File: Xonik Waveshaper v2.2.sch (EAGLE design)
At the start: 96 parts, among them IC1 TL074JT, IC2 TL074JT, IC3 TL074JT, IC4 TL072JT, IC5 4013T, IC6 LM311T, T1 2n3904

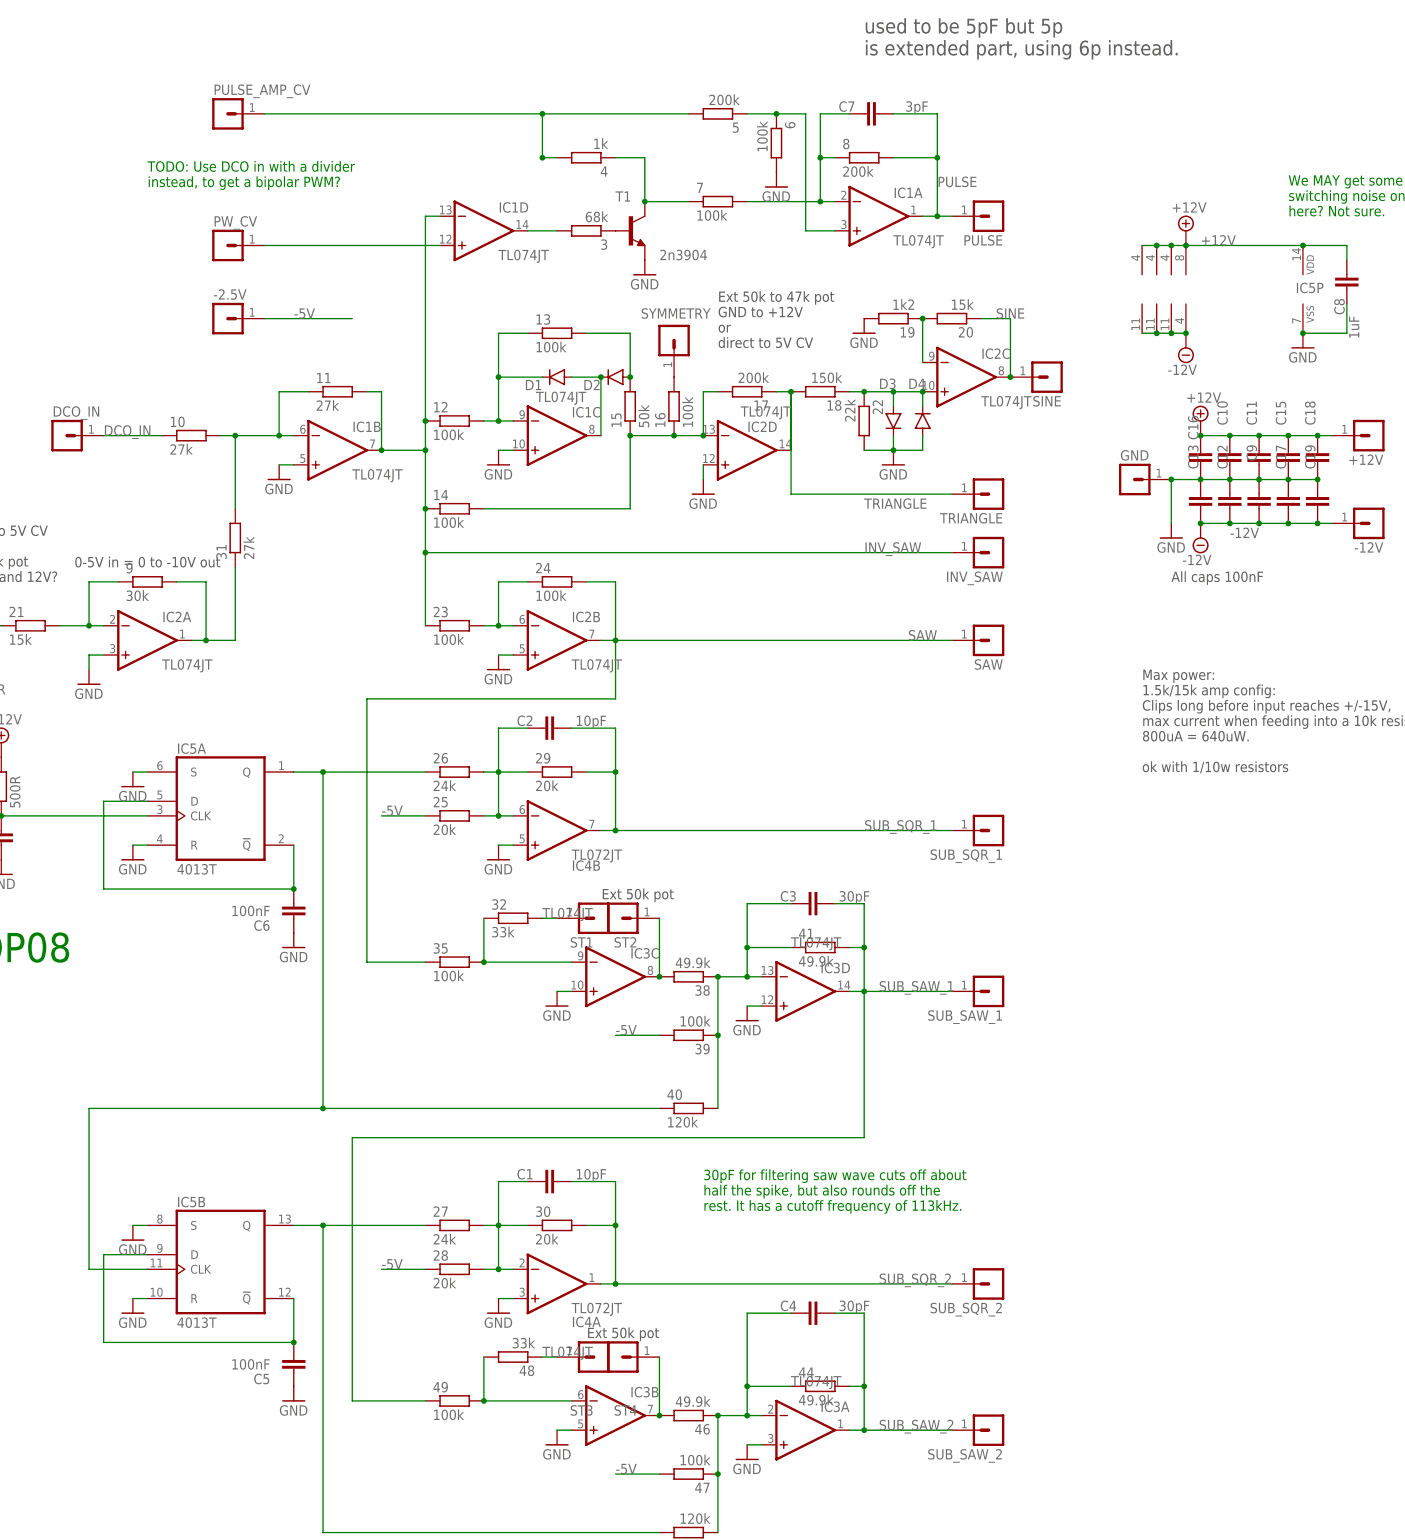
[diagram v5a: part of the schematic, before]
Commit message: Updated with bipolar pwm
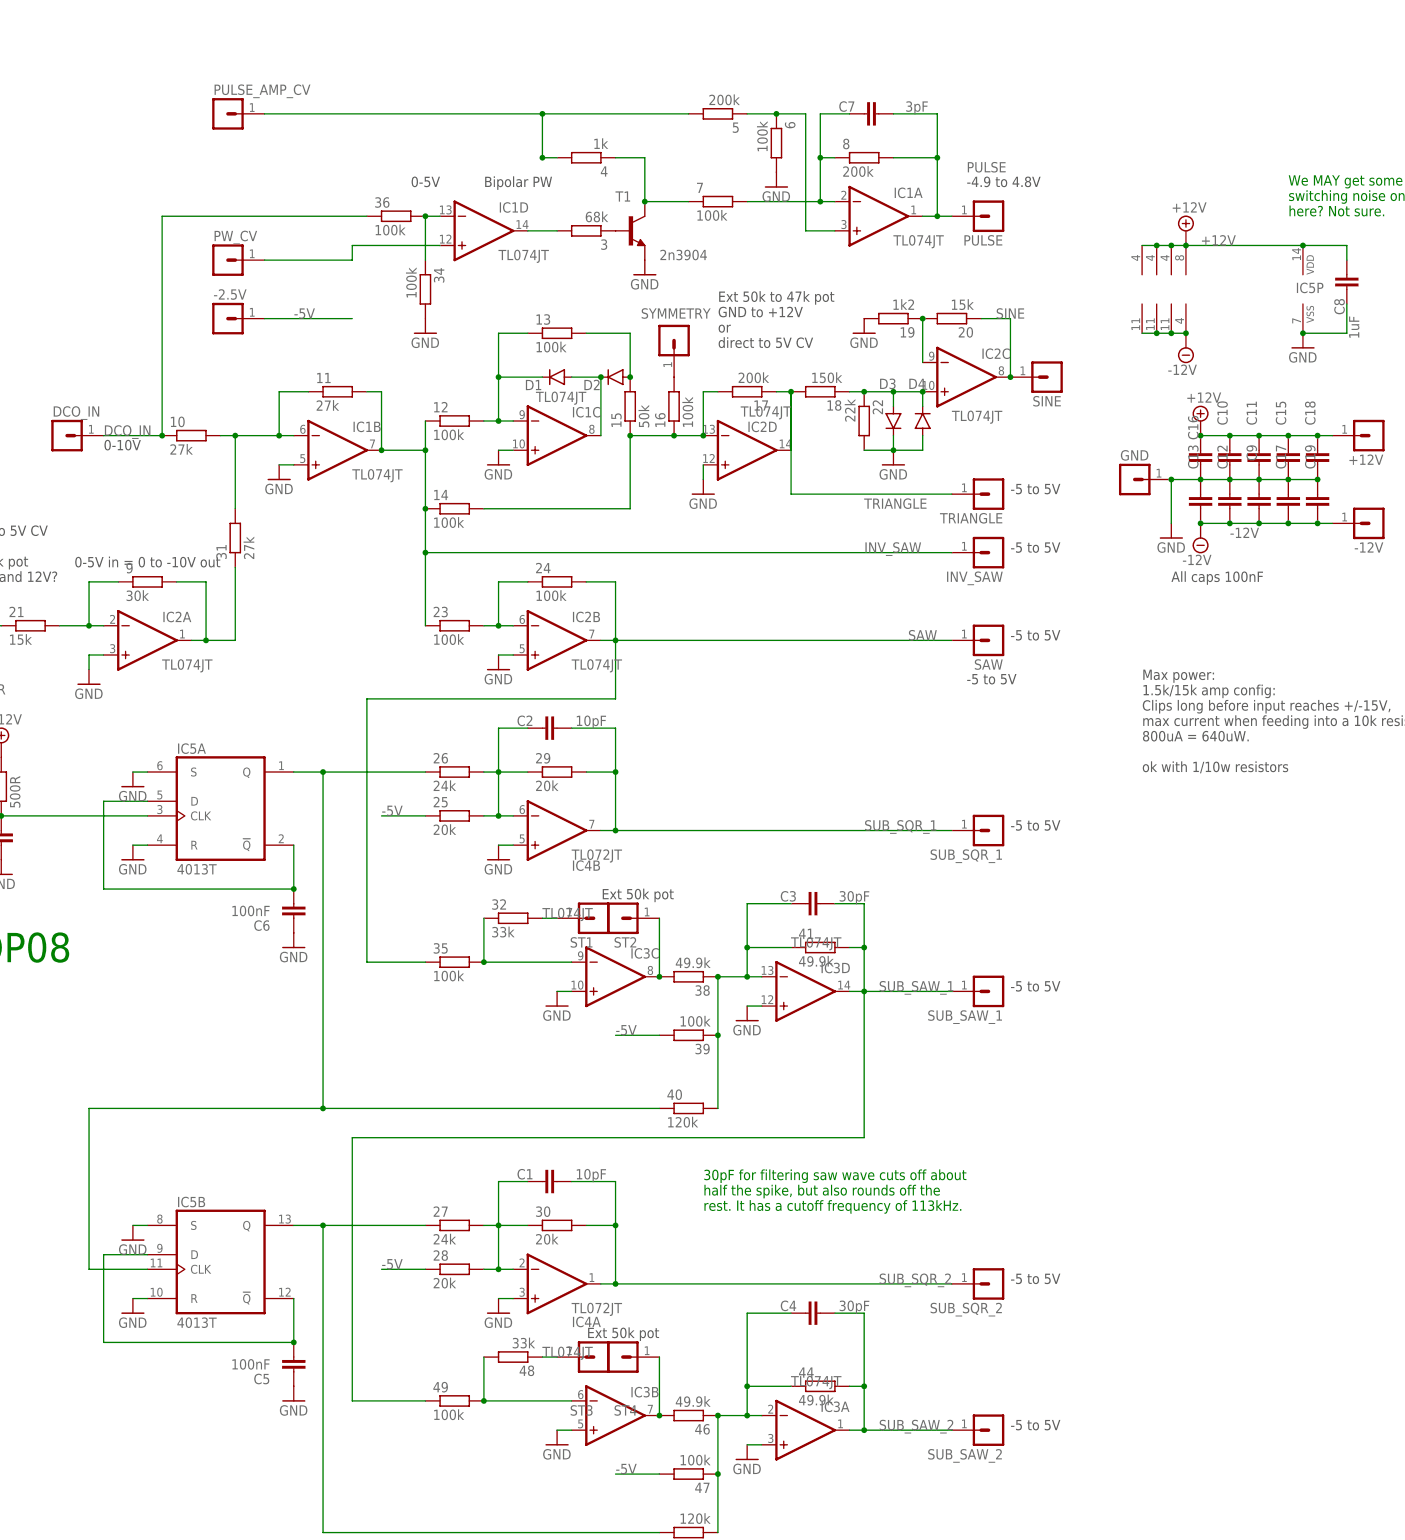
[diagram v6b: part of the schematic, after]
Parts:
- added 34, 36: 100k, rcl:R-EU_R0402
- 13, 24: device rcl:R-EU_R0603 -> rcl:R-EU_R0402
- C10, C11, C12, C13, C15, C16, C17, C18, C19, C8, C9: device rcl:C-EUC0402 -> joakim:C-EU-J0402
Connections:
- new net N$8: 34.1, 36.2, IC1D.-IN
- net DCO_IN: now also 36.1
- net GND: now also 34.2
- net INV_SAW: no longer IC1D.-IN
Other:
- note added: "-4.9 to 4.8V"
- note added: "-5 to 5V"
- note added: "0-10V"
- note added: "0-5V"
- note added: "Bipolar PW"
- note removed: "TODO: Use DCO in with a divider instead, to get a bipolar PWM?"
- note removed: "used to be 5pF but 5p is extended part, using 6p instead."
- moved on the sheet: PW_CV

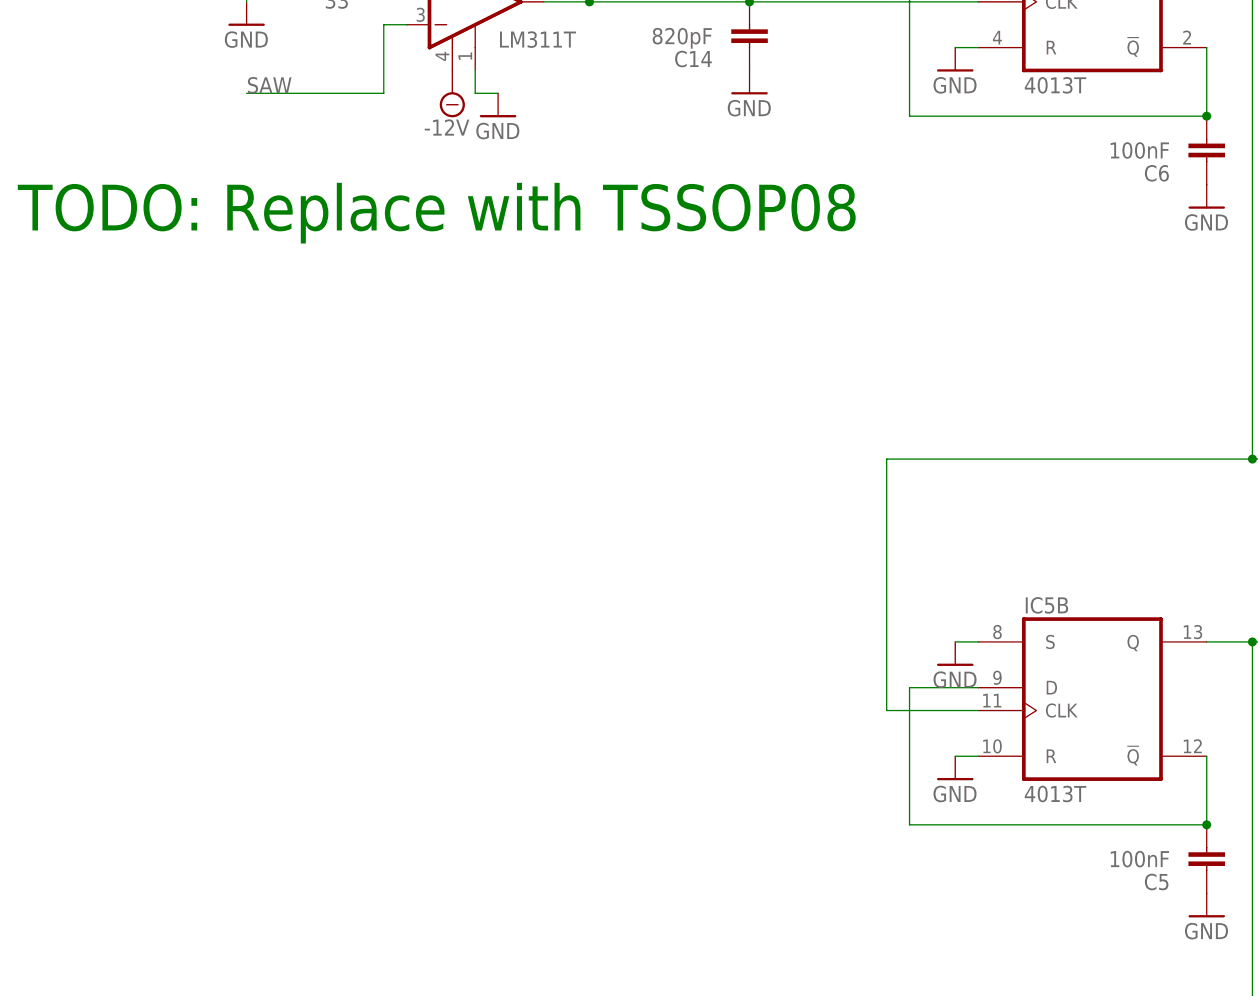
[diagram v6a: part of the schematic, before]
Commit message: prepared for single connector
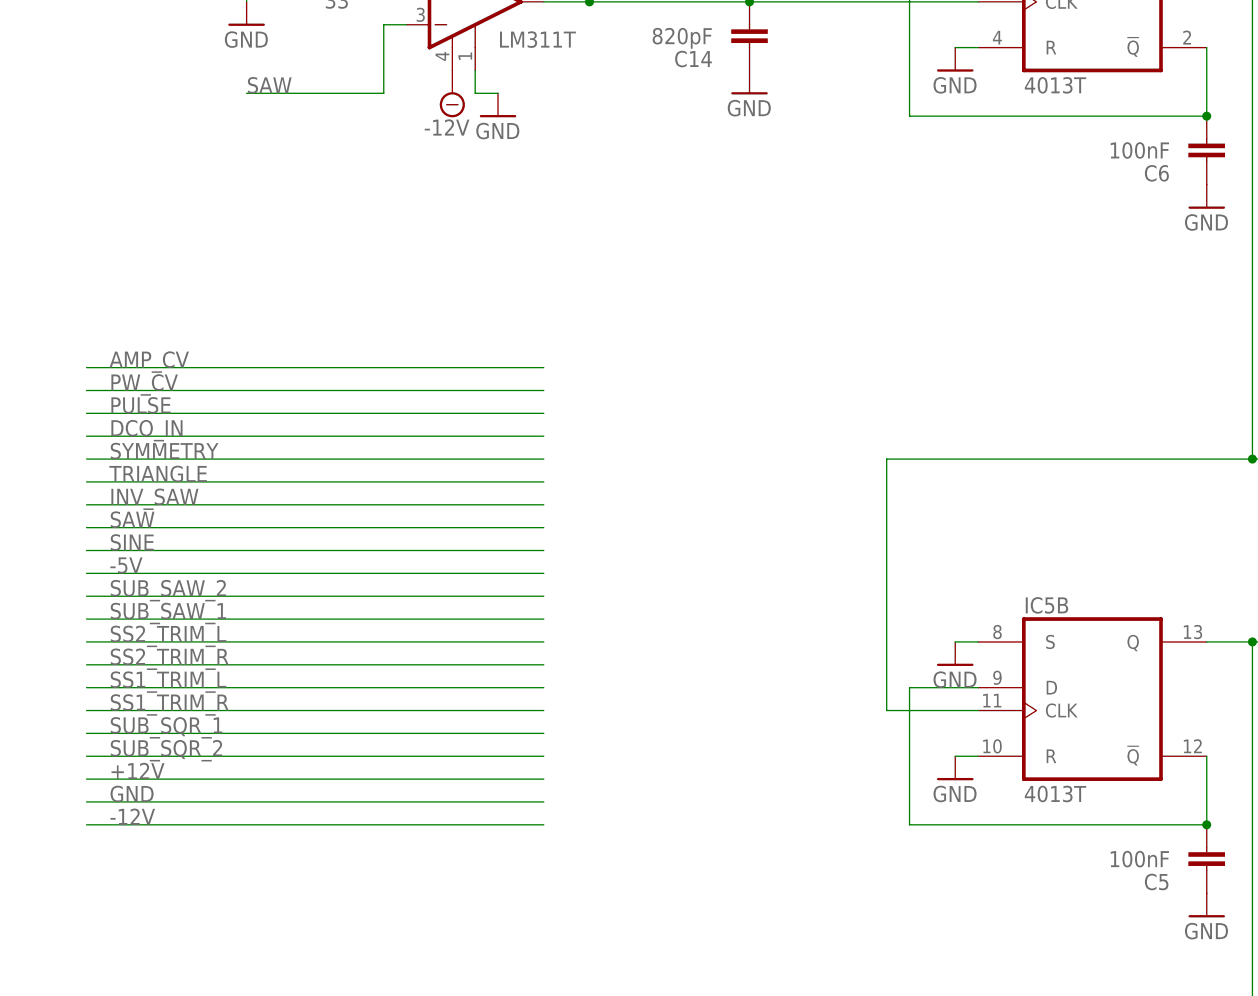
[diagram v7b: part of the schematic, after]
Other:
- note removed: "TODO: Replace with TSSOP08"
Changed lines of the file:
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@@
 switching noise on the analog 12V
 here? Not sure.</text>
-<text x="-154.94" y="-43.18" size="5.08" layer="91">TODO: Replace with TSSOP08</text>
 <text x="-55.88" y="45.72" size="1.778" layer="97">0-10V</text>
 <text x="-2.54" y="91.44" size="1.778" layer="97">0-5V</text>
@@
 <pinref part="GND25" gate="1" pin="GND"/>
 </segment>
+<segment>
+<wire x1="-147.32" y1="-106.68" x2="-96.52" y2="-106.68" width="0.1524" layer="91"/>
+<label x="-144.78" y="-106.68" size="1.778" layer="95"/>
+</segment>
 </net>
 <net name="N$2" class="0">
@@
 <pinref part="PULSE_AMP_CV" gate="G$1" pin="1"/>
 <junction x="20.32" y="104.14"/>
+</segment>
+<segment>
+<wire x1="-147.32" y1="-58.42" x2="-96.52" y2="-58.42" width="0.1524" layer="91"/>
+<label x="-144.78" y="-58.42" size="1.778" layer="95"/>
 </segment>
 </net>
@@
 <label x="93.98" y="93.98" size="1.778" layer="95"/>
 <pinref part="IC1" gate="A" pin="OUT"/>
+</segment>
+<segment>
+<wire x1="-147.32" y1="-63.5" x2="-96.52" y2="-63.5" width="0.1524" layer="91"/>
+<label x="-144.78" y="-63.5" size="1.778" layer="95"/>
 </segment>
 </net>
@@
 <junction x="-7.62" y="45.72"/>
 </segment>
+<segment>
+<wire x1="-147.32" y1="-73.66" x2="-96.52" y2="-73.66" width="0.1524" layer="91"/>
+<label x="-144.78" y="-73.66" size="1.778" layer="95"/>
+</segment>
 </net>
 <net name="N$10" class="0">
@@
 <pinref part="36" gate="G$1" pin="1"/>
 <wire x1="-45.72" y1="86.36" x2="-10.16" y2="86.36" width="0.1524" layer="91"/>
+</segment>
+<segment>
+<wire x1="-147.32" y1="-66.04" x2="-96.52" y2="-66.04" width="0.1524" layer="91"/>
+<label x="-144.78" y="-66.04" size="1.778" layer="95"/>
 </segment>
 </net>
@@
 <label x="76.2" y="-20.32" size="1.778" layer="95"/>
 </segment>
+<segment>
+<wire x1="-147.32" y1="-99.06" x2="-96.52" y2="-99.06" width="0.1524" layer="91"/>
+<label x="-144.78" y="-99.06" size="1.778" layer="95"/>
+</segment>
 </net>
 <net name="SUB_SQR_2" class="0">
@@
 <pinref part="SUB_SQR_2" gate="G$1" pin="1"/>
 <label x="78.74" y="-99.06" size="1.778" layer="95"/>
+</segment>
+<segment>
+<wire x1="-147.32" y1="-101.6" x2="-96.52" y2="-101.6" width="0.1524" layer="91"/>
+<label x="-144.78" y="-101.6" size="1.778" layer="95"/>
 </segment>
 </net>
@@
 <label x="78.74" y="-48.26" size="1.778" layer="95"/>
 </segment>
+<segment>
+<wire x1="-147.32" y1="-86.36" x2="-96.52" y2="-86.36" width="0.1524" layer="91"/>
+<label x="-144.78" y="-86.36" size="1.778" layer="95"/>
+</segment>
 </net>
 <net name="-5V" class="0">
@@
 <wire x1="-12.7" y1="68.58" x2="-27.94" y2="68.58" width="0.1524" layer="91"/>
 <label x="-22.86" y="68.58" size="1.778" layer="95"/>
+</segment>
+<segment>
+<wire x1="-147.32" y1="-81.28" x2="-96.52" y2="-81.28" width="0.1524" layer="91"/>
+<label x="-144.78" y="-81.28" size="1.778" layer="95"/>
 </segment>
 </net>
@@
 <pinref part="ST4" gate="G$1" pin="1"/>
 <wire x1="40.64" y1="-111.76" x2="40.64" y2="-121.92" width="0.1524" layer="91"/>
+</segment>
+<segment>
+<wire x1="-147.32" y1="-91.44" x2="-96.52" y2="-91.44" width="0.1524" layer="91"/>
+<label x="-144.78" y="-91.44" size="1.778" layer="95"/>
 </segment>
 </net>
@@
 <label x="78.74" y="-124.46" size="1.778" layer="95"/>
 </segment>
+<segment>
+<wire x1="-147.32" y1="-83.82" x2="-96.52" y2="-83.82" width="0.1524" layer="91"/>
+<label x="-144.78" y="-83.82" size="1.778" layer="95"/>
+</segment>
 </net>
 <net name="N$31" class="0">
@@
 <label x="76.2" y="35.56" size="1.778" layer="95"/>
 </segment>
+<segment>
+<wire x1="-147.32" y1="-71.12" x2="-96.52" y2="-71.12" width="0.1524" layer="91"/>
+<label x="-144.78" y="-71.12" size="1.778" layer="95"/>
+</segment>
 </net>
 <net name="N$39" class="0">
@@
 <junction x="101.6" y="58.42"/>
 <label x="99.06" y="68.58" size="1.778" layer="95"/>
+</segment>
+<segment>
+<wire x1="-147.32" y1="-78.74" x2="-96.52" y2="-78.74" width="0.1524" layer="91"/>
+<label x="-144.78" y="-78.74" size="1.778" layer="95"/>
 </segment>
 </net>
@@
 <pinref part="SUPPLY2" gate="+12V" pin="+12V"/>
 </segment>
+<segment>
+<wire x1="-147.32" y1="-104.14" x2="-96.52" y2="-104.14" width="0.1524" layer="91"/>
+<label x="-144.78" y="-104.14" size="1.778" layer="95"/>
+</segment>
 </net>
 <net name="SYMMETRY" class="0">
@@
 <pinref part="16" gate="G$1" pin="2"/>
 <pinref part="SYMMETRY" gate="G$1" pin="1"/>
+</segment>
+<segment>
+<wire x1="-147.32" y1="-68.58" x2="-96.52" y2="-68.58" width="0.1524" layer="91"/>
+<label x="-144.78" y="-68.58" size="1.778" layer="95"/>
 </segment>
 </net>
@@
 <pinref part="ST2" gate="G$1" pin="1"/>
 <wire x1="40.64" y1="-35.56" x2="40.64" y2="-45.72" width="0.1524" layer="91"/>
+</segment>
+<segment>
+<wire x1="-147.32" y1="-96.52" x2="-96.52" y2="-96.52" width="0.1524" layer="91"/>
+<label x="-144.78" y="-96.52" size="1.778" layer="95"/>
 </segment>
 </net>
@@
 <pinref part="SUPPLY3" gate="G$1" pin="-12V"/>
 </segment>
+<segment>
+<wire x1="-147.32" y1="-109.22" x2="-96.52" y2="-109.22" width="0.1524" layer="91"/>
+<label x="-144.78" y="-109.22" size="1.778" layer="95"/>
+</segment>
 </net>
 <net name="PW_CV" class="0">
@@
 <wire x1="-12.7" y1="81.28" x2="2.54" y2="81.28" width="0.1524" layer="91"/>
 <pinref part="IC1" gate="D" pin="+IN"/>
+</segment>
+<segment>
+<wire x1="-147.32" y1="-60.96" x2="-96.52" y2="-60.96" width="0.1524" layer="91"/>
+<label x="-144.78" y="-60.96" size="1.778" layer="95"/>
 </segment>
 </net>
@@
 <wire x1="20.32" y1="-35.56" x2="22.86" y2="-35.56" width="0.1524" layer="91"/>
 </segment>
+<segment>
+<wire x1="-147.32" y1="-93.98" x2="-96.52" y2="-93.98" width="0.1524" layer="91"/>
+<label x="-144.78" y="-93.98" size="1.778" layer="95"/>
+</segment>
 </net>
 <net name="SS2_TRIM_L" class="0">
@@
 <pinref part="48" gate="G$1" pin="1"/>
 <wire x1="22.86" y1="-111.76" x2="20.32" y2="-111.76" width="0.1524" layer="91"/>
+</segment>
+<segment>
+<wire x1="-147.32" y1="-88.9" x2="-96.52" y2="-88.9" width="0.1524" layer="91"/>
+<label x="-144.78" y="-88.9" size="1.778" layer="95"/>
 </segment>
 </net>
@@
 <pinref part="IC2" gate="B" pin="OUT"/>
 </segment>
-</net>
+<segment>
+<wire x1="-147.32" y1="-76.2" x2="-96.52" y2="-76.2" width="0.1524" layer="91"/>
+<label x="-144.78" y="-76.2" size="1.778" layer="95"/>
+</segment>
+</net>
